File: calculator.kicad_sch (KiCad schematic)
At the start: 9 parts, among them J1 NHD-0216CW-AB3, J2 Conn_01x20_Socket, U1 STM32F103RETx

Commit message: Design more of the pcb
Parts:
- removed J1: NHD-0216CW-AB3, NHD0216CWAB3, symbol NHD-0216CW-AB3:NHD-0216CW-AB3
- added BT1: Battery, symbol Device:Battery
- added C10, C11, C12, C13, C14, C15, C16, C17, C18, C19, C20, C21, C7, C8, C9: C, symbol Device:C
- added D1: LED, symbol Device:LED
- added D2: D, symbol Device:D
- added J1: Conn_01x04_Pin, symbol Connector:Conn_01x04_Pin
- added R1: R, symbol Device:R
- added SW1, SW10, SW2, SW3, SW4, SW5, SW6, SW7, SW8, SW9: SW_Push, symbol Switch:SW_Push
- added U2: AMS1117, Package_TO_SOT_SMD:SOT-223-3_TabPin2, symbol Regulator_Linear:AMS1117
- added Y1: Crystal, symbol Device:Crystal
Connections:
- net OLED_BS0 is gone; now on net GND: J2.17 (Pin_17)
- net OLED_BS1 is gone; now on net +3V3: J2.18 (Pin_18)
- net OLED_BS2 is gone; now on net GND: J2.19 (Pin_19)
- net OLED_CS is gone; now on net GND: J2.15 (Pin_15)
- net OLED_D0 is gone; now on net OLED_SCL: J2.7 (Pin_7)
- net OLED_D1 is gone; now on net OLED_SDA: J2.8 (Pin_8)
- net OLED_D2 is gone; now on net OLED_SDA: J2.9 (Pin_9)
- net OLED_D3 is gone; now on net GND: J2.10 (Pin_10)
- net OLED_D4 is gone; now on net GND: J2.11 (Pin_11)
- net OLED_D5 is gone; now on net GND: J2.12 (Pin_12)
- net OLED_D6 is gone; now on net GND: J2.13 (Pin_13)
- net OLED_D7 is gone; now on net GND: J2.14 (Pin_14)
- net OLED_D/C is gone; now on net OLED_SA0: J2.4 (Pin_4)
- net OLED_REGVDD is gone; now on net GND: J2.3 (Pin_3)
- net OLED_VDD is gone; now on net +3V3: J2.2 (Pin_2)
- net OLED_VSS is gone; now on net GND: J2.1 (Pin_1)
- net OLED_VSS2 is gone; now on net GND: J2.20 (Pin_20)
- net +3V3: now also C11.1, D2.1 (K), R1.1, SW1.1, SW10.1, SW2.1, SW3.1, SW4.1, SW5.1, SW6.1, SW7.1, SW8.1, SW9.1, U2.2 (VO)
- net GND: now also BT1.2 (-), C10.1, C11.2, C12.2, C13.2, C14.2, C15.2, C16.2, C17.2, C18.2, C19.2, C20.2, C21.2, C7.1, C8.1, C9.2, D1.1 (K), J1.1 (Pin_1), U2.1 (ADJ)
- net OLED_RES: now also U1.55 (PB3)
- net SWDIO: now reaches U1.46 (PA13)
- net SWDIO: now also J1.3 (Pin_3)
- net SWDCLK: now reaches U1.49 (PA14)
- net SWDCLK: now also J1.2 (Pin_2)
- net OLED_SA0: now reaches U1.56 (PB4)
- net OLED_SCL: now reaches U1.58 (PB6)
- net OLED_SDA: now reaches U1.59 (PB7)
- net OLED_E: no longer names the net of J2.6 (Pin_6)
- net OLED_R/W: no longer names the net of J2.5 (Pin_5)
- new net: D1.2 (A), R1.2
- new net: BT1.1 (+), D2.2 (A)
- new net +5V: C10.2, C9.1, J1.4 (Pin_4), U2.3 (VI)
- new net 0: C21.1, SW10.2
- new net 1: C12.1, SW1.2
- new net 2: C19.1, SW8.2
- new net 3: C20.1, SW9.2
- new net 4: C16.1, SW5.2
- new net 5: C17.1, SW6.2
- new net 6: C18.1, SW7.2
- new net 7: C13.1, SW2.2
- new net 8: C14.1, SW3.2
- new net 9: C15.1, SW4.2
- new net OSC_IN: C7.2, Y1.1
- new net OSC_OUT: C8.2, Y1.2
- no-connect marks 0 -> 2

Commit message: Design more of the pcb
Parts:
- added C22, C23, C24, C25, C26, C27, C28, C29, C30, C31, C32: C, symbol Device:C
- added SW11, SW12, SW13, SW14, SW15, SW16, SW17, SW18, SW19, SW20, SW21: SW_Push, symbol Switch:SW_Push
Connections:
- net +3V3: now also SW11.1, SW12.1, SW13.1, SW14.1, SW15.1, SW16.1, SW17.1, SW18.1, SW19.1, SW20.1, SW21.1
- net GND: now also C22.2, C23.2, C24.2, C25.2, C26.2, C27.2, C28.2, C30.2, C31.2
- net 0 renamed BUT_1
- net 1 renamed BUT_4
- net 2 renamed BUT_5
- net 3 renamed BUT_6
- net 4 renamed BUT_7
- net 5 renamed BUT_8
- net 6 renamed BUT_9
- net 7 renamed BUT_ON
- net 8 renamed BUT_DEL
- net 9 renamed BUT_CLEAR
- new net BUT_0: C22.1, SW11.2
- new net BUT_2: C25.1, SW14.2
- new net BUT_3: C26.1, SW15.2
- new net BUT_DIV: C28.1, SW17.2
- new net BUT_DOT: C23.1, SW12.2
- new net BUT_MIN: C27.1, SW16.2
- new net BUT_MULT: C29.1, C32.1, SW18.2, SW21.2
- new net BUT_PLUS: C24.1, SW13.2
- new net BUT_SQARE: C31.1, SW20.2
- new net BUT_SQRT: C30.1, SW19.2
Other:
- moved on the sheet: C14, C15, C17, C18, C19, C20, SW3, SW4, SW6, SW7, SW8, SW9

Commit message: STACK-46 Implement state reporting
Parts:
- removed D2: D, symbol Device:D
- added C33, C34, C35, C36, C37, C38: 100nF, Capacitor_SMD:C_0603_1608Metric, symbol Device:C
- added C39: 2.2uF, Capacitor_SMD:C_0603_1608Metric, symbol Device:C
- added C40: 47uF, Capacitor_SMD:C_0805_2012Metric, symbol Device:C
- added C41: 10uF, Capacitor_SMD:C_0603_1608Metric, symbol Device:C
- added L1: 6.8uH, symbol Device:L
- added R2, R3, R4, R5, R6: R, symbol Device:R
- added SW22, SW23, SW24, SW25, SW26, SW27: SW_Push, symbol Switch:SW_Push
- added U3: TPS61025DRCR, DRC0010J, symbol DRC0010J:TPS61025DRCR
- C1, C10, C11, C12, C13, C14, C15, C16, C17, C18, C19, C2, C20, C21, C22, C23, C24, C25, C26, C27, C28, C29, C3, C30, C31, C32, C4, C5, C6, C9: value C -> 100nF; footprint (none) -> Capacitor_SMD:C_0603_1608Metric
- C7, C8: value C -> 20pF; footprint (none) -> Capacitor_SMD:C_0603_1608Metric
- D1: footprint (none) -> LED_SMD:LED_0603_1608Metric
- J1: footprint (none) -> Connector_PinHeader_2.54mm:PinHeader_1x04_P2.54mm_Vertical
- Y1: value Crystal -> 8Mhz; footprint (none) -> Crystal:Crystal_SMD_HC49-SD
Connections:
- net BUT_0 is gone; now on net COL_1: C22.1, SW11.2
- net BUT_1 is gone; now on net COL_1: C21.1, SW10.2
- net BUT_2 is gone; now on net COL_2: C25.1, SW14.2
- net BUT_3 is gone; now on net COL_3: C26.1, SW15.2
- net BUT_4 is gone; now on net COL_1: C12.1, SW1.2
- net BUT_5 is gone; now on net COL_2: C19.1, SW8.2
- net BUT_7 is gone; now on net COL_1: C16.1, SW5.2
- net BUT_8 is gone; now on net COL_2: C17.1, SW6.2
- net BUT_9 is gone; now on net COL_3: C18.1, SW7.2
- net BUT_CLEAR is gone; now on net COL_3: C15.1, SW4.2
- net BUT_DEL is gone; now on net COL_2: C14.1, SW3.2
- net BUT_DIV is gone; now on net COL_2: C28.1, SW17.2
- net BUT_DOT is gone; now on net COL_2: C23.1, SW12.2
- net BUT_MIN is gone; now on net COL_1: C27.1, SW16.2
- net BUT_ON is gone; now on net COL_1: C13.1, SW2.2
- net BUT_PLUS is gone; now on net COL_3: C24.1, SW13.2
- net BUT_SQARE is gone; now on net COL_2: C31.1, SW20.2
- net BUT_SQRT is gone; now on net COL_1: C30.1, SW19.2
- net +3V3: now also C39.1, C40.1, R2.1, R6.1, U3.2 (VOUT); no longer SW1.1, SW10.1, SW11.1, SW12.1, SW13.1, SW14.1, SW15.1, SW16.1, SW17.1, SW18.1, SW19.1, SW2.1, SW20.1, SW21.1, SW3.1, SW4.1, SW5.1, SW6.1, SW7.1, SW8.1, SW9.1
- net GND: now also C29.2, C32.2, C33.2, C34.2, C35.2, C36.2, C37.2, C38.2, C39.2, C40.2, C41.2, R3.2, R5.2, U3.10 (PGND), U3.11 (PAD), U3.5 (GND), U3.8 (PS)
- net COL_3: now reaches U1.10 (PC2)
- net COL_3: now also C32.1, SW21.2, C35.1, C38.1, SW24.2, SW27.2
- net ROW_1: now reaches U1.11 (PC3)
- net ROW_1: now also SW2.1, SW3.1, SW4.1
- net ROW_2: now reaches U1.24 (PC4)
- net ROW_2: now also SW5.1, SW6.1, SW7.1
- net ROW_3: now reaches U1.25 (PC5)
- net ROW_3: now also SW1.1, SW8.1, SW9.1
- net ROW_4: now reaches U1.37 (PC6)
- net ROW_4: now also SW10.1, SW14.1, SW15.1
- net ROW_5: now reaches U1.38 (PC7)
- net ROW_5: now also SW11.1, SW12.1, SW13.1
- net ROW_6: now reaches U1.39 (PC8)
- net ROW_6: now also SW16.1, SW17.1, SW18.1
- net ROW_7: now reaches U1.40 (PC9)
- net ROW_7: now also SW19.1, SW20.1, SW21.1
- net ROW_8: now reaches U1.51 (PC10)
- net ROW_8: now also SW22.1, SW23.1, SW24.1
- net ROW_9: now reaches U1.52 (PC11)
- net ROW_9: now also SW25.1, SW26.1, SW27.1
- net COL_1: now reaches U1.8 (PC0)
- net COL_1: now also C33.1, C36.1, SW22.2, SW25.2
- net COL_2: now reaches U1.9 (PC1)
- net COL_2: now also C34.1, C37.1, SW23.2, SW26.2
- net +3V0: now reaches BT1.1 (+)
- net +3V0: now also C41.1, L1.2, R4.1, U3.1 (EN), U3.6 (VBAT)
- net BUT_MULT renamed v
- net v: no longer C32.1, SW21.2
- new net: R2.2, R3.1, U3.3 (FB)
- new net: L1.1, U3.9 (SW)
- new net: R4.2, R5.1, U3.7 (LBI)
- new net LOW_BATTERY: R6.2, U3.4 (LBO)
- no-connect marks 2 -> 3
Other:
- moved on the sheet: BT1

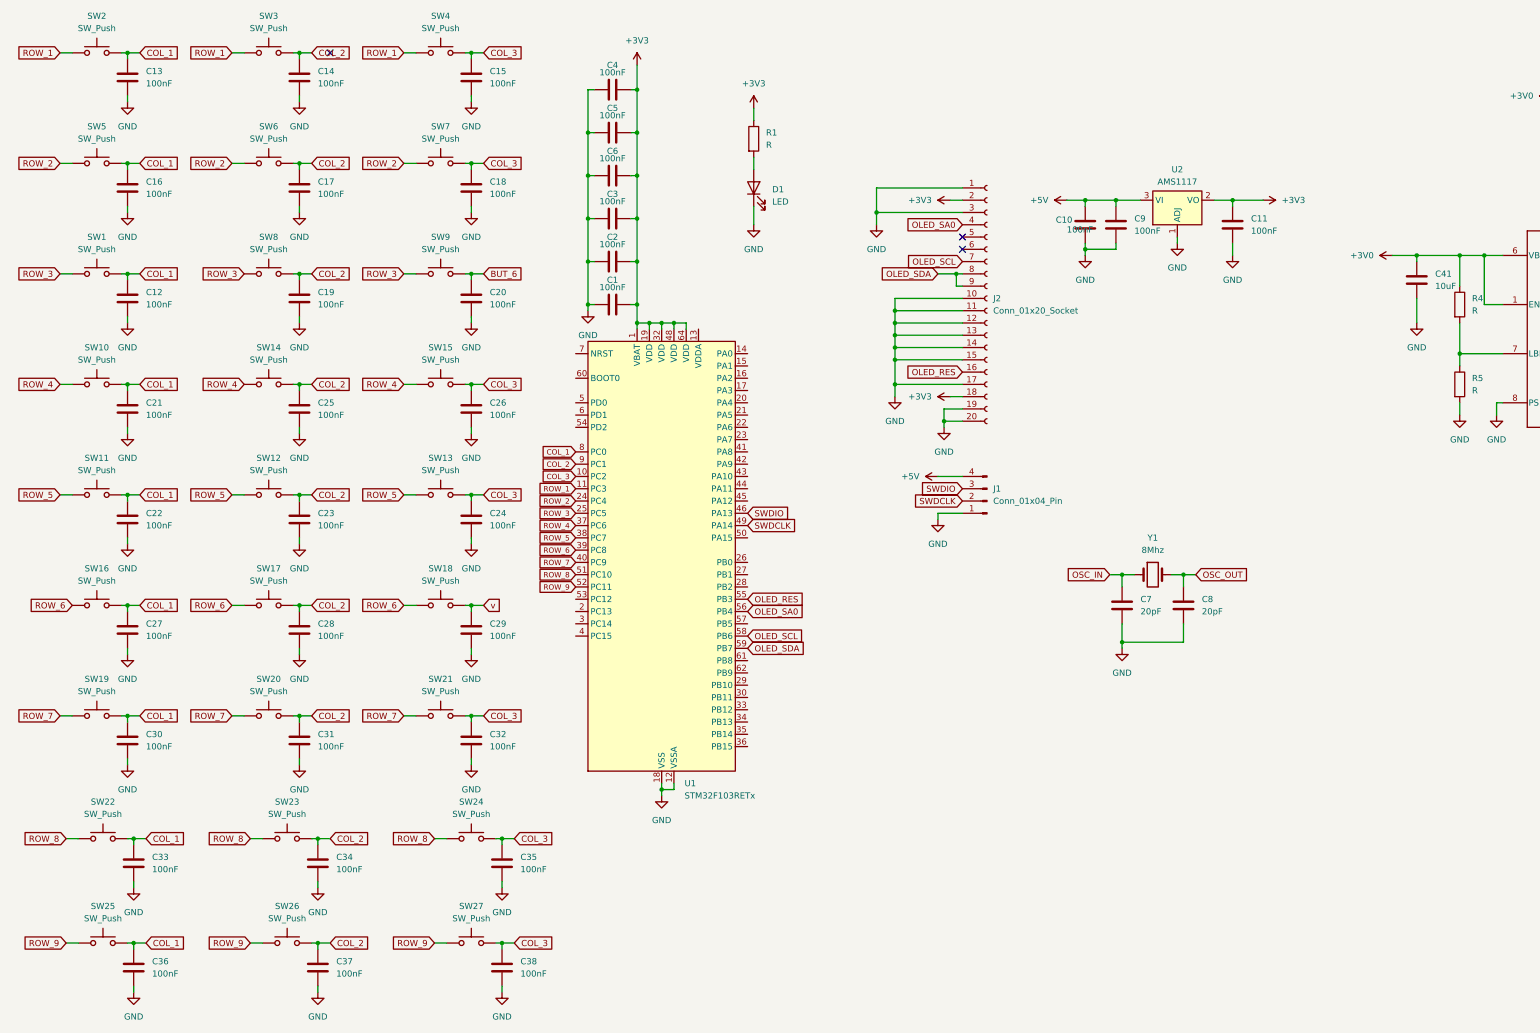
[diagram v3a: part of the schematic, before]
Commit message: Finish schematic design
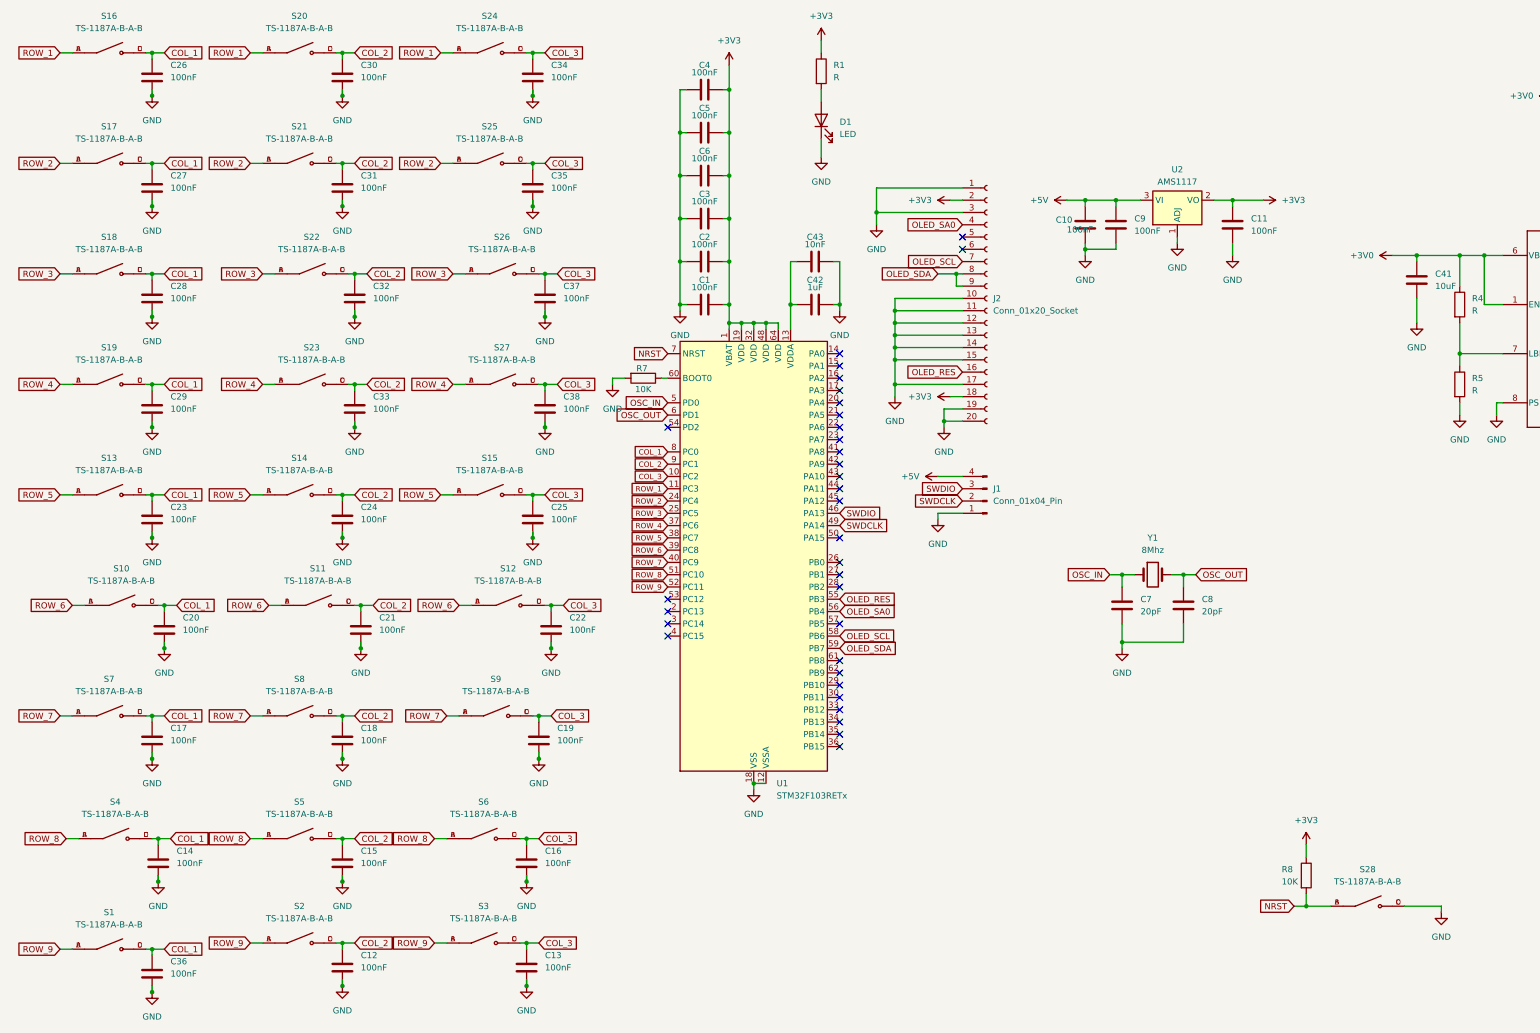
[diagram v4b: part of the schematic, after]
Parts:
- removed SW1, SW10, SW11, SW12, SW13, SW14, SW15, SW16, SW17, SW18, SW19, SW2, SW20, SW21, SW22, SW23, SW24, SW25, SW26, SW27, SW3, SW4, SW5, SW6, SW7, SW8, SW9: SW_Push, symbol Switch:SW_Push
- added C42: 1uF, Capacitor_SMD:C_0603_1608Metric, symbol Device:C
- added C43: 10nF, Capacitor_SMD:C_0603_1608Metric, symbol Device:C
- added R7, R8: 10K, Resistor_SMD:R_0201_0603Metric, symbol Device:R
- added S1, S10, S11, S12, S13, S14, S15, S16, S17, S18, S19, S2, S20, S21, S22, S23, S24, S25, S26, S27, S28, S3, S4, S5, S6, S7, S8, S9: TS-1187A-B-A-B, TS-1187A-B-A-B:SW_TS-1187A-B-A-B, symbol TS-1187A-B-A-B:TS-1187A-B-A-B
- BT1: footprint (none) -> Battery_Pads:Battery_Pads
- L1: footprint (none) -> IND_NP-4R7NC_SUM:IND_NP-4R7NC_SUM
- R1, R2, R3, R4, R5, R6: footprint (none) -> Resistor_SMD:R_0201_0603Metric
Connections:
- net BUT_6 is gone; now on net COL_1: C20.1
- net v is gone; now on net COL_1: C29.1
- net +3V3: now also R8.1
- net COL_1: now also C14.1, C17.1, C23.1, C26.1, C28.1, S1.C, S1.D, S10.C, S10.D, S13.C, S13.D, S16.C, S16.D, S17.C, S17.D, S18.C, S18.D, S19.C, S19.D, S4.C, S4.D, S7.C, S7.D; no longer C12.1, C13.1, C16.1, C21.1, C22.1, C30.1, C33.1
- net COL_2: now also C12.1, C15.1, C18.1, C21.1, C24.1, C30.1, C32.1, C33.1, S11.C, S11.D, S14.C, S14.D, S2.C, S2.D, S20.C, S20.D, S21.C, S21.D, S22.C, S22.D, S23.C, S23.D, S5.C, S5.D, S8.C, S8.D; no longer C14.1, C17.1, C19.1, C23.1, C25.1, C28.1, C34.1, C37.1
- net COL_3: now also C13.1, C16.1, C19.1, C22.1, C25.1, C34.1, C37.1, S12.C, S12.D, S15.C, S15.D, S24.C, S24.D, S25.C, S25.D, S26.C, S26.D, S27.C, S27.D, S3.C, S3.D, S6.C, S6.D, S9.C, S9.D; no longer C15.1, C18.1, C24.1, C26.1, C32.1
- net GND: now also C42.2, C43.2, R7.2, S28.C, S28.D
- net OSC_IN: now also U1.5 (PD0)
- net OSC_OUT: now also U1.6 (PD1)
- net ROW_1: now also S16.A, S16.B, S20.A, S20.B, S24.A, S24.B
- net ROW_2: now also S17.A, S17.B, S21.A, S21.B, S25.A, S25.B
- net ROW_3: now also S18.A, S18.B, S22.A, S22.B, S26.A, S26.B
- net ROW_4: now also S19.A, S19.B, S23.A, S23.B, S27.A, S27.B
- net ROW_5: now also S13.A, S13.B, S14.A, S14.B, S15.A, S15.B
- net ROW_6: now also S10.A, S10.B, S11.A, S11.B, S12.A, S12.B
- net ROW_7: now also S7.A, S7.B, S8.A, S8.B, S9.A, S9.B
- net ROW_8: now also S4.A, S4.B, S5.A, S5.B, S6.A, S6.B
- net ROW_9: now also S1.A, S1.B, S2.A, S2.B, S3.A, S3.B
- net at U1.13 (VDDA): now also C42.1, C43.1
- net at U1.60 (BOOT0): now also R7.1
- net NRST: now reaches U1.7 (NRST)
- net NRST: now also R8.2, S28.A, S28.B
- no-connect marks 3 -> 33
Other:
- moved on the sheet: C1, C2, C3, C36, C4, C5, C6, D1, R1, U1
